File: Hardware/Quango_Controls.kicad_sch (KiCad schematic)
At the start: 33 parts, among them J1 Conn_01x12_Male, J10 Gate_Out, J2 Conn_01x16_Male, J3 Conn_01x12_Male, J4 Conn_01x12_Male, J5 CV_A, J6 CV_B, J7 Out, J8 USB_C_Receptacle, J9 Midi_In, SW1 SW_Push, SW2 SW_Push

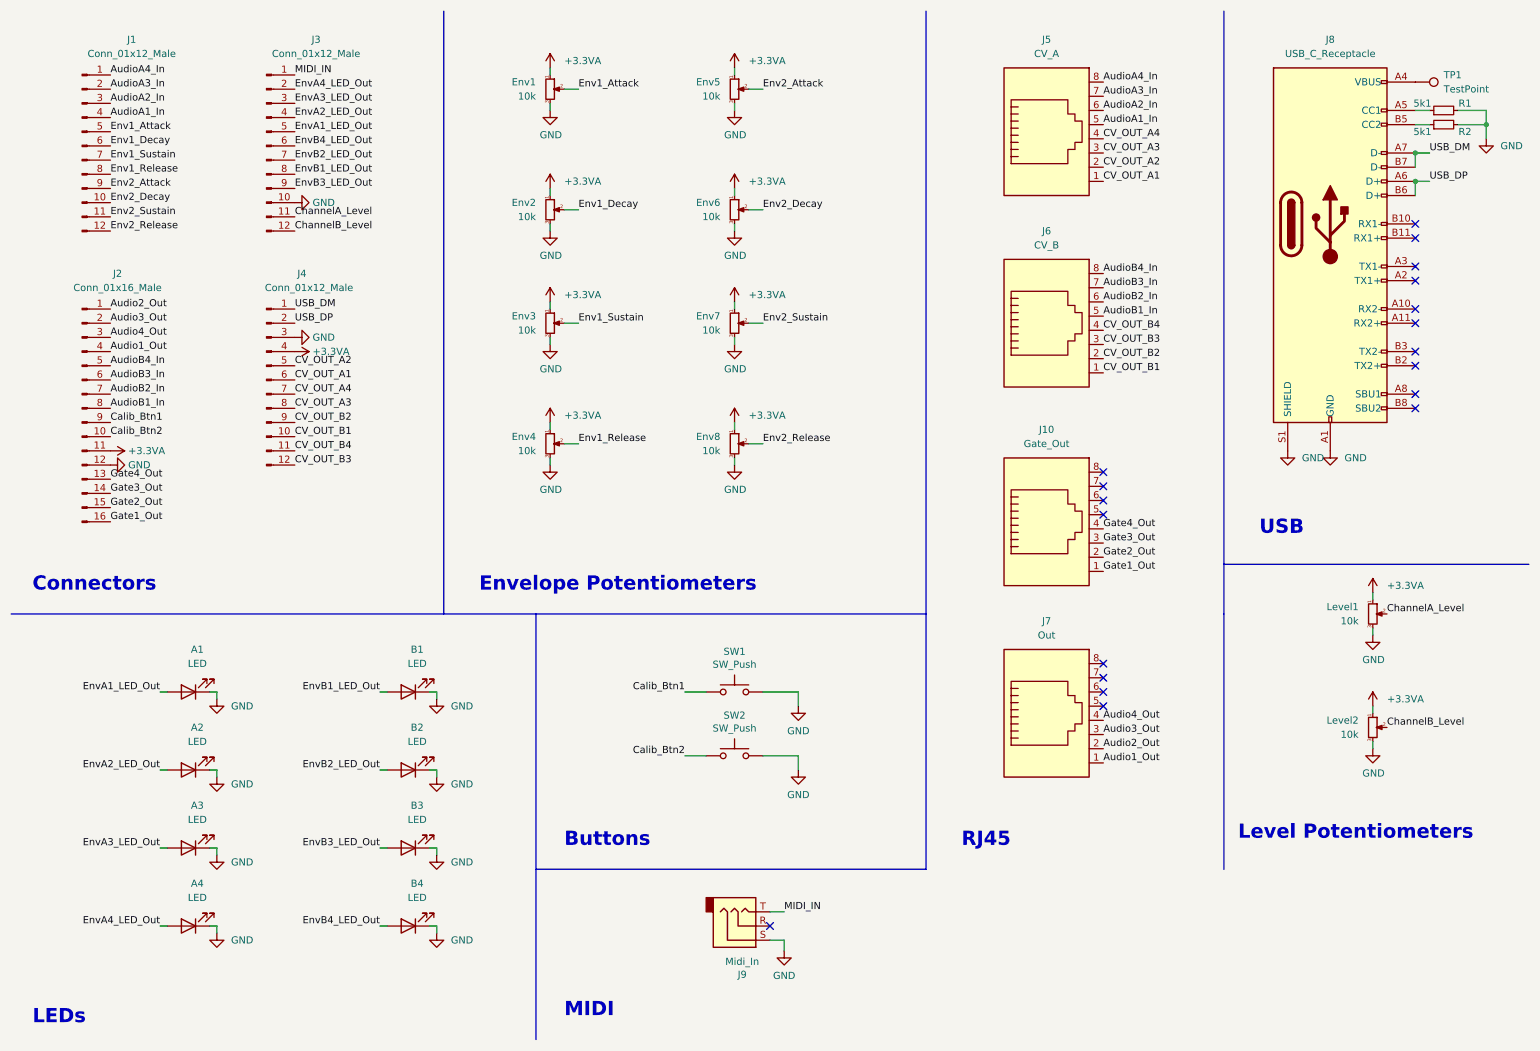
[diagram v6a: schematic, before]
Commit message: Updated controls to include octave switching; revised panel
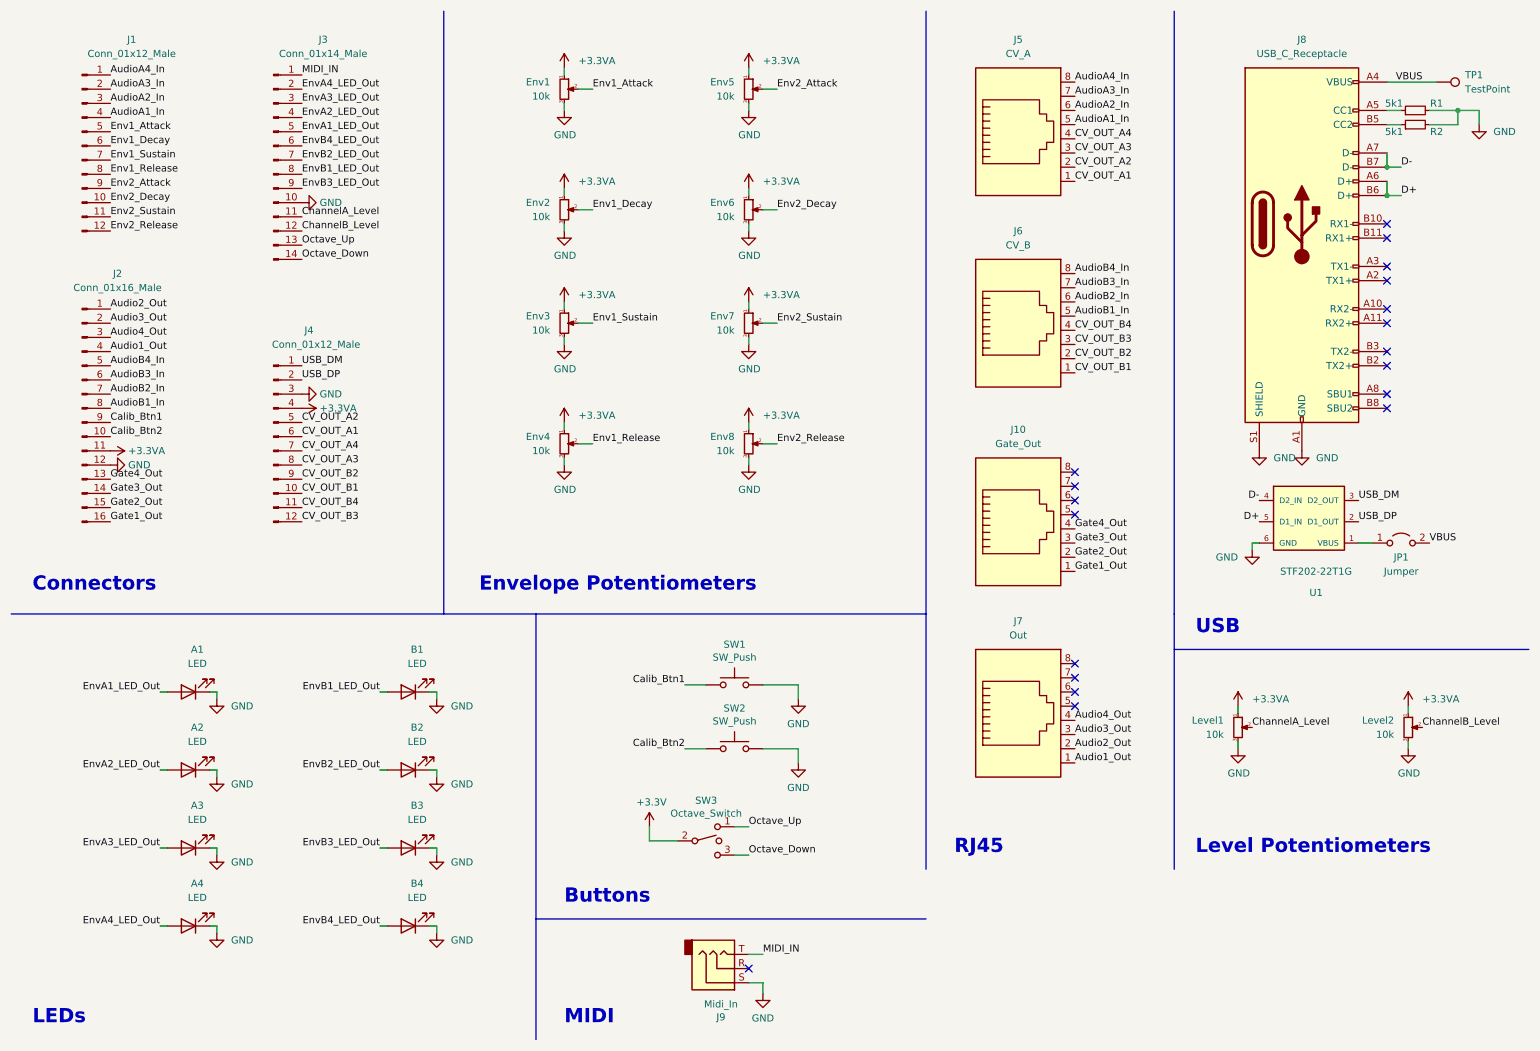
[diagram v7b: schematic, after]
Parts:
- removed J3: Conn_01x12_Male, Connector_PinSocket_2.54mm:PinSocket_1x12_P2.54mm_Vertical, symbol Connector:Conn_01x12_Male
- added J3: Conn_01x14_Male, Connector_PinSocket_2.54mm:PinSocket_1x14_P2.54mm_Vertical, symbol Connector:Conn_01x14_Male
- added JP1: Jumper, Jumper:SolderJumper-2_P1.3mm_Open_RoundedPad1.0x1.5mm, symbol Jumper:Jumper_2_Open
- added SW3: Octave_Switch, Custom_Footprints:SP3T_Mini_Switch, symbol Switch:SW_SPDT_MSM
- added U1: STF202-22T1G, Custom_Footprints:STF202-22T1G, symbol STF202-22T1G:STF202-22T1G
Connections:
- net ChannelA_Level: now also J3.11 (Pin_11)
- net ChannelB_Level: now also J3.12 (Pin_12)
- net EnvA1_LED_Out: now also J3.5 (Pin_5)
- net EnvA2_LED_Out: now also J3.4 (Pin_4)
- net EnvA3_LED_Out: now also J3.3 (Pin_3)
- net EnvA4_LED_Out: now also J3.2 (Pin_2)
- net EnvB1_LED_Out: now also J3.8 (Pin_8)
- net EnvB2_LED_Out: now also J3.7 (Pin_7)
- net EnvB3_LED_Out: now also J3.9 (Pin_9)
- net EnvB4_LED_Out: now also J3.6 (Pin_6)
- net GND: now also J3.10 (Pin_10), U1.6 (GND)
- net MIDI_IN: now also J3.1 (Pin_1)
- net USB_DM: now also U1.3 (D2_OUT); no longer J8.A7 (D-), J8.B7 (D-)
- net USB_DP: now also U1.2 (D1_OUT); no longer J8.A6 (D+), J8.B6 (D+)
- net VBUS: now reaches J8.A4 (VBUS), J8.A9 (VBUS), J8.B4 (VBUS), J8.B9 (VBUS), TP1.1
- net VBUS: now also JP1.2 (B)
- new net: JP1.1 (A), U1.1 (VBUS)
- new net +3V3: SW3.2
- new net D+: J8.A6 (D+), J8.B6 (D+), U1.5 (D1_IN)
- new net D-: J8.A7 (D-), J8.B7 (D-), U1.4 (D2_IN)
- new net Octave_Down: J3.14 (Pin_14), SW3.3
- new net Octave_Up: J3.13 (Pin_13), SW3.1
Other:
- company: (none) -> Mountjoy Modular
- title: (none) -> Quango Controls
- moved on the sheet: Env1, Env2, Env3, Env4, Env5, Env6, Env7, Env8, J10, J4, J5, J6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

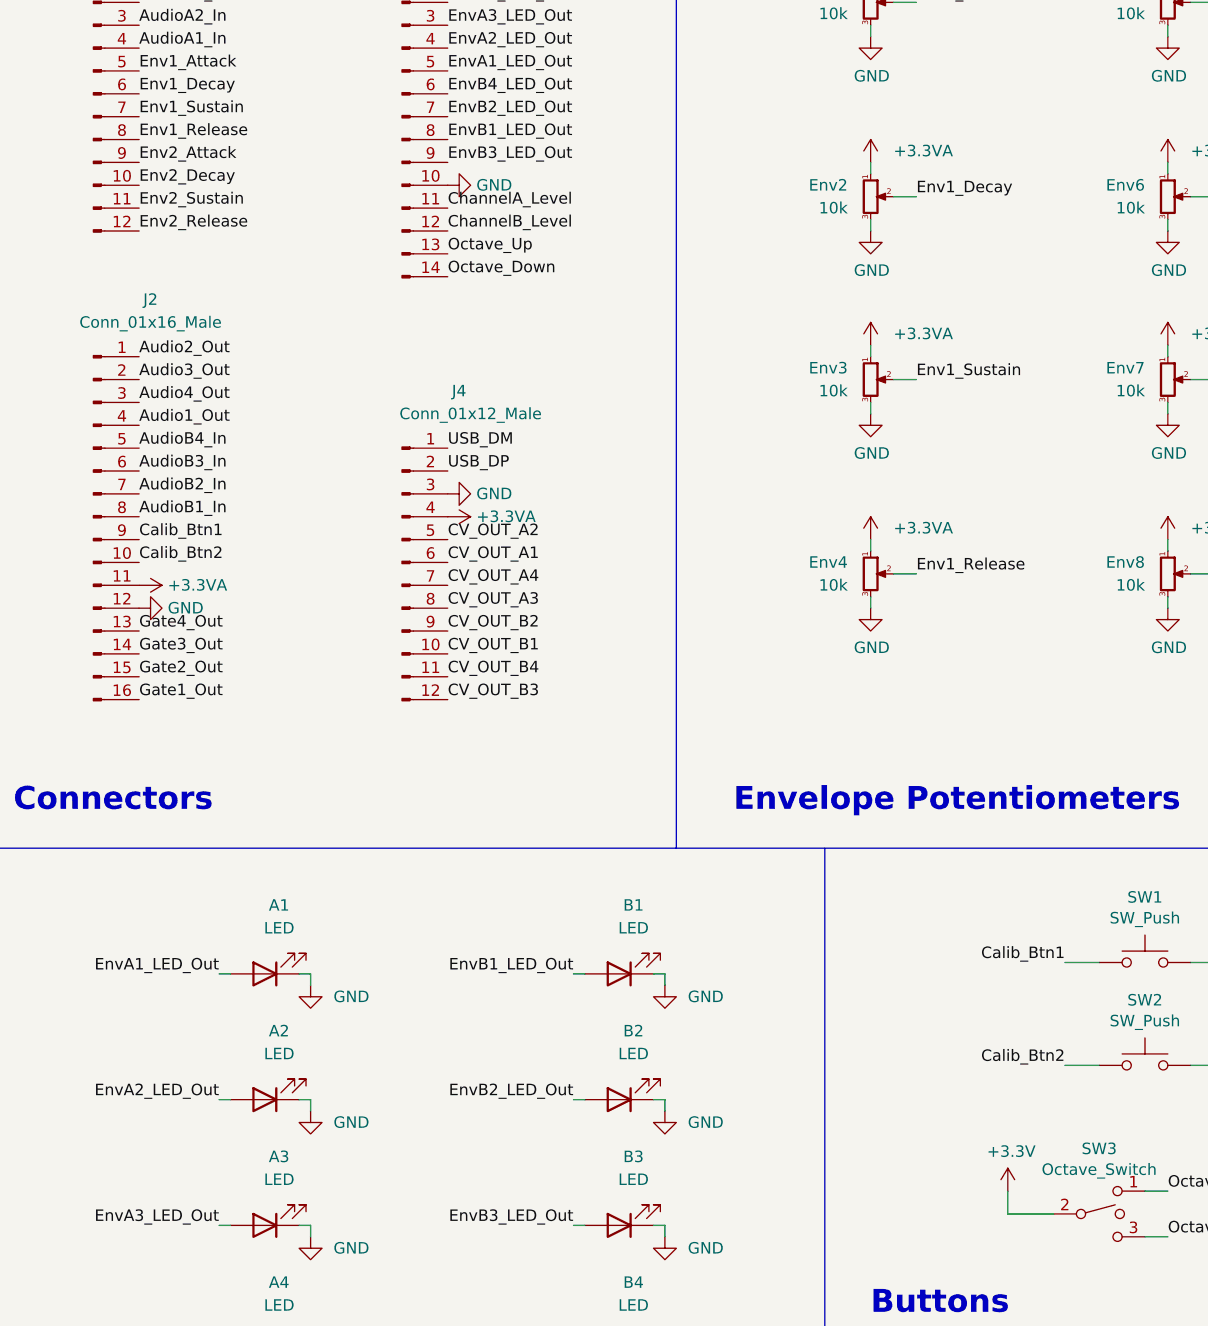
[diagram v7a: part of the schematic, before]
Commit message: Prepared v2 controls and panel for  manufacture
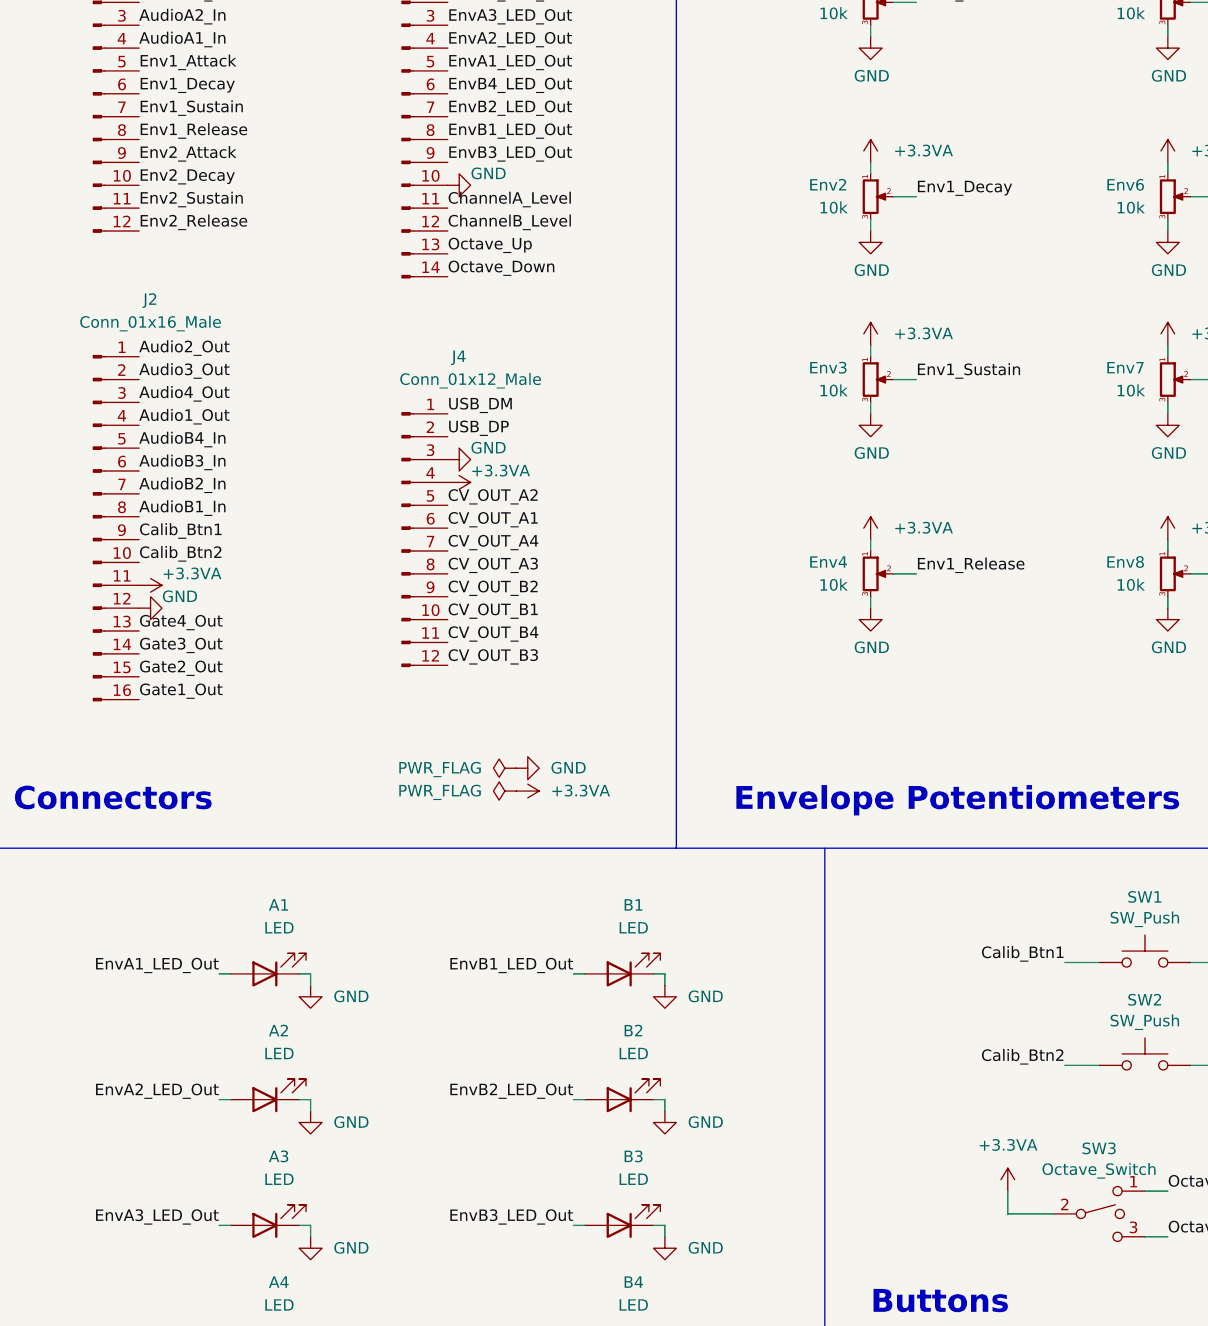
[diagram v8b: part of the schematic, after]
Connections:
- net +3V3 is gone; now on net +3.3VA: SW3.2
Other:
- moved on the sheet: J4
